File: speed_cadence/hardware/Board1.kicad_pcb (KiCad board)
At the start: 2 copper layers, 32.8 x 58.2 mm, 17 parts, among them IC1 AH1912-W-7, J1 DX07S016JA3R1500, J2 Conn_01x04_Pin, J3 Conn_ST_STDC14, J4 XT60_M_7.2mm, SW1 SW_Push, U1 STM32F042G6U6TR, U2 TS2940CW33_RPG

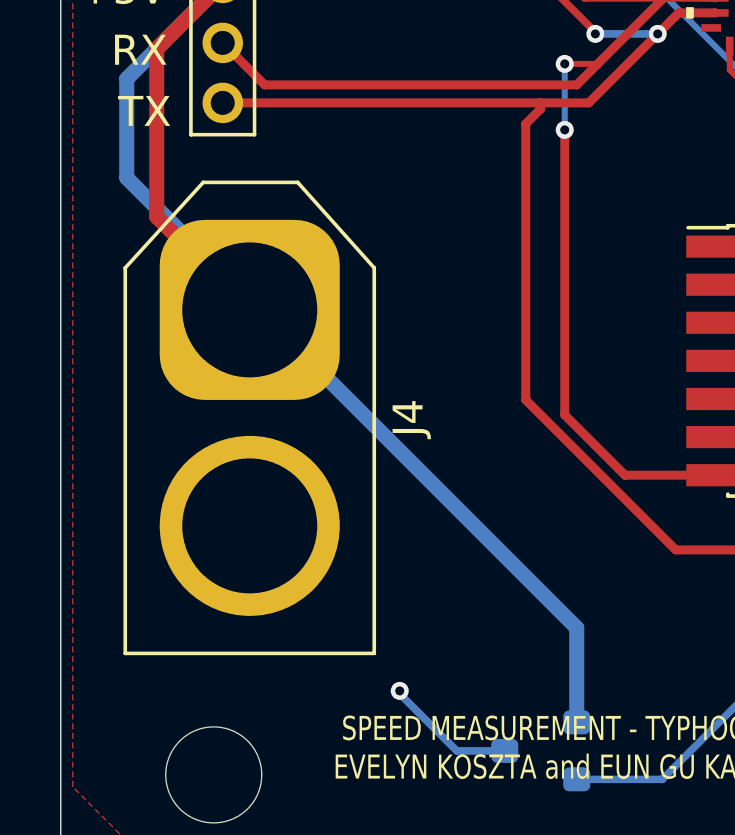
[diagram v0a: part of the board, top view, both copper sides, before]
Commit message: flipped connector
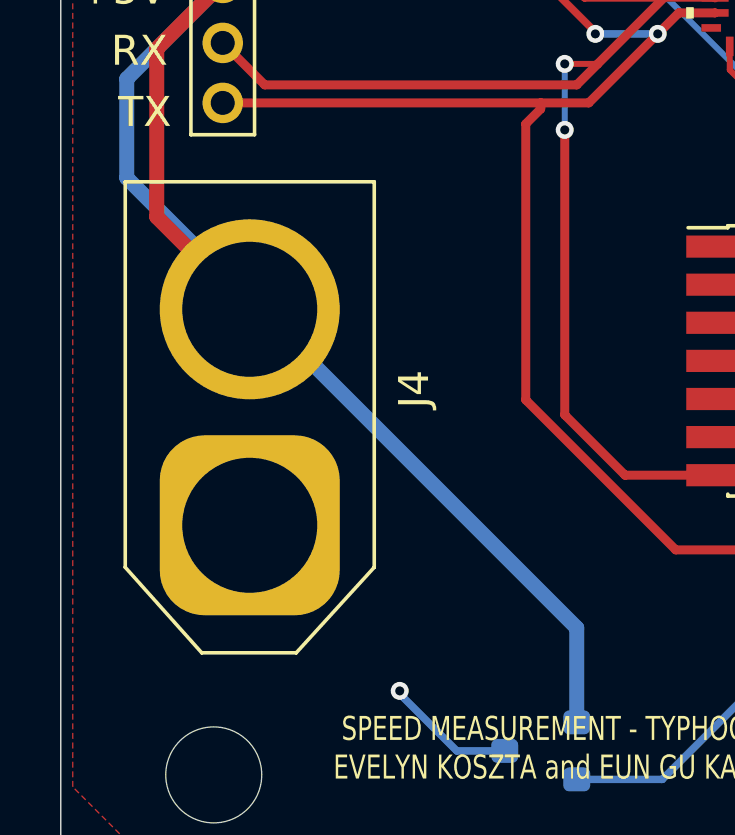
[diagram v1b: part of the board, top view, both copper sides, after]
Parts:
- moved J4 7.18 mm to (75.1, 97.1), turned to 90 degrees
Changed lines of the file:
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@@
 	(footprint "Connector_AMASS:AMASS_XT60-M_1x02_P7.20mm_Vertical"
 		(layer "F.Cu")
-		(at 75.1 89.9 -90)
+		(at 75.1 97.08 90)
 		(descr "AMASS female XT60, through hole, vertical, https://www.tme.eu/Document/2d152ced3b7a446066e6c419d84bb460/XT60%20SPEC.pdf")
 		(tags "XT60 female vertical")
 		(property "Reference" "J4"
-			(at 3.6 -5.3 90)
+			(at 4.54 5.48 270)
 			(layer "F.SilkS")
 			(effects
@@
 		)
 		(property "Value" "XT60_M_7.2mm"
-			(at 3.6 5.4 90)
+			(at 3.6 5.4 270)
 			(layer "F.Fab")
 			(effects
@@
 		)
 		(property "Footprint" "Connector_AMASS:AMASS_XT60-M_1x02_P7.20mm_Vertical"
-			(at 0 0 -90)
+			(at 0 0 90)
 			(unlocked yes)
 			(layer "F.Fab")
@@
 		)
 		(property "Datasheet" ""
-			(at 0 0 -90)
+			(at 0 0 90)
 			(unlocked yes)
 			(layer "F.Fab")
@@
 		)
 		(property "Description" "Generic connector, single row, 01x02, script generated"
-			(at 0 0 -90)
+			(at 0 0 90)
 			(unlocked yes)
 			(layer "F.Fab")
@@
 		(attr through_hole)
 		(fp_line
+			(start 11.45 -4.15)
+			(end -1.4 -4.15)
+			(stroke
+				(width 0.12)
+				(type solid)
+			)
+			(layer "F.SilkS")
+		)
+		(fp_line
+			(start -1.4 -4.15)
+			(end -4.25 -1.6)
+			(stroke
+				(width 0.12)
+				(type solid)
+			)
+			(layer "F.SilkS")
+		)
+		(fp_line
+			(start -4.25 -1.6)
+			(end -4.25 1.55)
+			(stroke
+				(width 0.12)
+				(type solid)
+			)
+			(layer "F.SilkS")
+		)
+		(fp_line
+			(start -4.25 1.55)
+			(end -1.4 4.15)
+			(stroke
+				(width 0.12)
+				(type solid)
+			)
+			(layer "F.SilkS")
+		)
+		(fp_line
+			(start 11.45 4.15)
+			(end 11.45 -4.15)
+			(stroke
+				(width 0.12)
+				(type solid)
+			)
+			(layer "F.SilkS")
+		)
+		(fp_line
 			(start -1.4 4.15)
 			(end 11.45 4.15)
@@
 		)
 		(fp_line
-			(start 11.45 4.15)
-			(end 11.45 -4.15)
-			(stroke
-				(width 0.12)
-				(type solid)
-			)
-			(layer "F.SilkS")
-		)
-		(fp_line
-			(start -4.25 1.55)
-			(end -1.4 4.15)
-			(stroke
-				(width 0.12)
-				(type solid)
-			)
-			(layer "F.SilkS")
-		)
-		(fp_line
-			(start -4.25 -1.6)
-			(end -4.25 1.55)
-			(stroke
-				(width 0.12)
-				(type solid)
-			)
-			(layer "F.SilkS")
-		)
-		(fp_line
-			(start -1.4 -4.15)
-			(end -4.25 -1.6)
-			(stroke
-				(width 0.12)
-				(type solid)
-			)
-			(layer "F.SilkS")
-		)
-		(fp_line
-			(start 11.45 -4.15)
-			(end -1.4 -4.15)
-			(stroke
-				(width 0.12)
-				(type solid)
-			)
-			(layer "F.SilkS")
+			(start 11.85 -4.6)
+			(end 11.85 4.6)
+			(stroke
+				(width 0.05)
+				(type solid)
+			)
+			(layer "F.CrtYd")
+		)
+		(fp_line
+			(start -1.6 -4.6)
+			(end 11.85 -4.6)
+			(stroke
+				(width 0.05)
+				(type solid)
+			)
+			(layer "F.CrtYd")
+		)
+		(fp_line
+			(start -4.65 -1.85)
+			(end -1.6 -4.6)
+			(stroke
+				(width 0.05)
+				(type solid)
+			)
+			(layer "F.CrtYd")
+		)
+		(fp_line
+			(start -4.65 1.85)
+			(end -4.65 -1.85)
+			(stroke
+				(width 0.05)
+				(type solid)
+			)
+			(layer "F.CrtYd")
+		)
+		(fp_line
+			(start 11.85 4.6)
+			(end -1.6 4.6)
+			(stroke
+				(width 0.05)
+				(type solid)
+			)
+			(layer "F.CrtYd")
 		)
 		(fp_line
@@
 		)
 		(fp_line
-			(start 11.85 4.6)
-			(end -1.6 4.6)
-			(stroke
-				(width 0.05)
-				(type solid)
-			)
-			(layer "F.CrtYd")
-		)
-		(fp_line
-			(start -4.65 1.85)
-			(end -4.65 -1.85)
-			(stroke
-				(width 0.05)
-				(type solid)
-			)
-			(layer "F.CrtYd")
-		)
-		(fp_line
-			(start -4.65 -1.85)
-			(end -1.6 -4.6)
-			(stroke
-				(width 0.05)
-				(type solid)
-			)
-			(layer "F.CrtYd")
-		)
-		(fp_line
-			(start -1.6 -4.6)
-			(end 11.85 -4.6)
-			(stroke
-				(width 0.05)
-				(type solid)
-			)
-			(layer "F.CrtYd")
-		)
-		(fp_line
-			(start 11.85 -4.6)
-			(end 11.85 4.6)
-			(stroke
-				(width 0.05)
-				(type solid)
-			)
-			(layer "F.CrtYd")
+			(start 11.35 -4.05)
+			(end -1.4 -4.05)
+			(stroke
+				(width 0.12)
+				(type solid)
+			)
+			(layer "F.Fab")
+		)
+		(fp_line
+			(start -1.4 -4.05)
+			(end -4.15 -1.55)
+			(stroke
+				(width 0.12)
+				(type solid)
+			)
+			(layer "F.Fab")
+		)
+		(fp_line
+			(start -4.15 -1.55)
+			(end -4.15 1.55)
+			(stroke
+				(width 0.12)
+				(type solid)
+			)
+			(layer "F.Fab")
+		)
+		(fp_line
+			(start -4.15 1.55)
+			(end -1.4 4.05)
+			(stroke
+				(width 0.12)
+				(type solid)
+			)
+			(layer "F.Fab")
+		)
+		(fp_line
+			(start 11.35 4.05)
+			(end 11.35 -4.05)
+			(stroke
+				(width 0.12)
+				(type solid)
+			)
+			(layer "F.Fab")
 		)
 		(fp_line
@@
 			(layer "F.Fab")
 		)
-		(fp_line
-			(start 11.35 4.05)
-			(end 11.35 -4.05)
-			(stroke
-				(width 0.12)
-				(type solid)
-			)
-			(layer "F.Fab")
-		)
-		(fp_line
-			(start -4.15 1.55)
-			(end -1.4 4.05)
-			(stroke
-				(width 0.12)
-				(type solid)
-			)
-			(layer "F.Fab")
-		)
-		(fp_line
-			(start -4.15 -1.55)
-			(end -4.15 1.55)
-			(stroke
-				(width 0.12)
-				(type solid)
-			)
-			(layer "F.Fab")
-		)
-		(fp_line
-			(start -1.4 -4.05)
-			(end -4.15 -1.55)
-			(stroke
-				(width 0.12)
-				(type solid)
-			)
-			(layer "F.Fab")
-		)
-		(fp_line
-			(start 11.35 -4.05)
-			(end -1.4 -4.05)
-			(stroke
-				(width 0.12)
-				(type solid)
-			)
-			(layer "F.Fab")
-		)
 		(fp_text user "${REFERENCE}"
-			(at 3.6 0.05 90)
+			(at 3.6 0.05 270)
 			(layer "F.Fab")
 			(effects
@@
 		)
 		(pad "1" thru_hole roundrect
-			(at 0 0 270)
+			(at 0 0 90)
 			(size 6 6)
 			(drill 4.5)
@@
 		)
 		(pad "2" thru_hole circle
-			(at 7.2 0 270)
+			(at 7.2 0 90)
 			(size 6 6)
 			(drill 4.5)

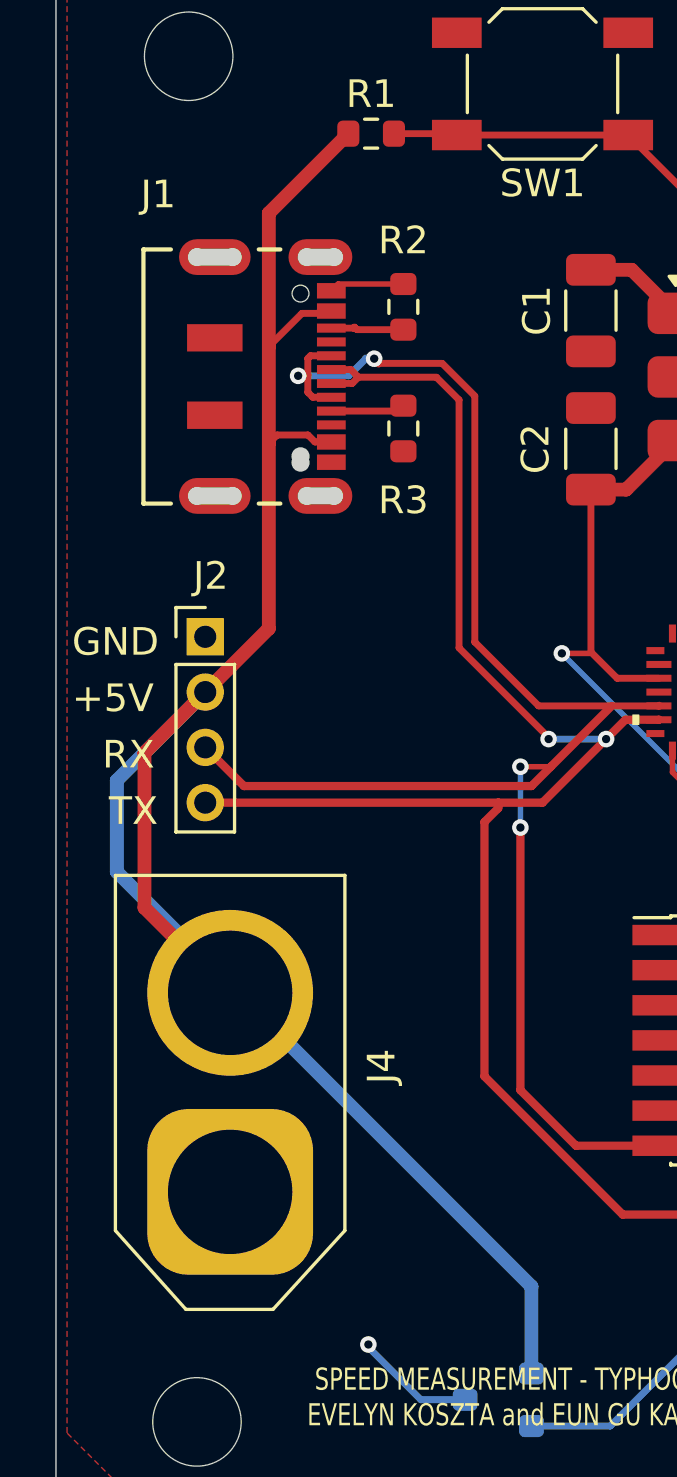
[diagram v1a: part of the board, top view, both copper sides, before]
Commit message: Removed battery connector
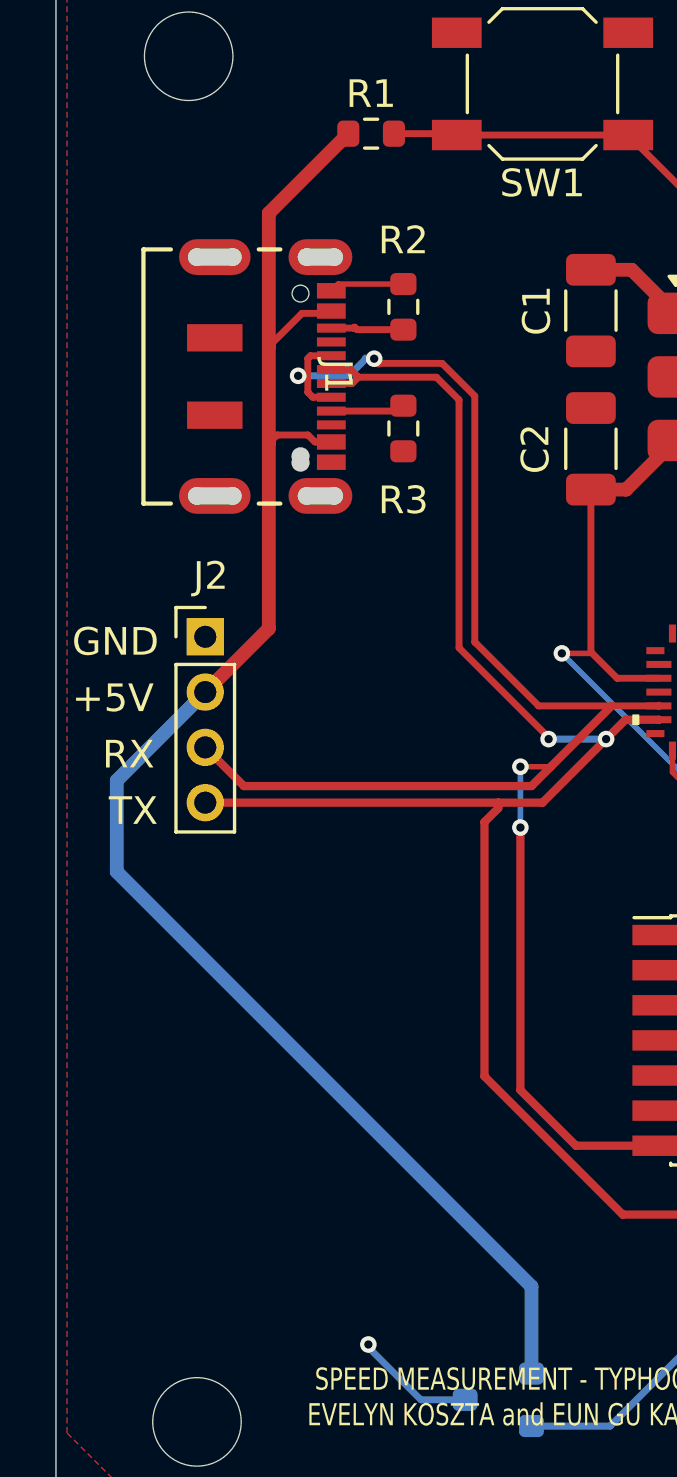
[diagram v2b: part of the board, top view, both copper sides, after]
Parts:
- removed J4: XT60_M_7.2mm, Connector_AMASS:AMASS_XT60-M_1x02_P7.20mm_Vertical
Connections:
- net + BATT renamed +5V
- net - BATT renamed GND
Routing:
- net +5V: track 76.6 -> 63.5 mm

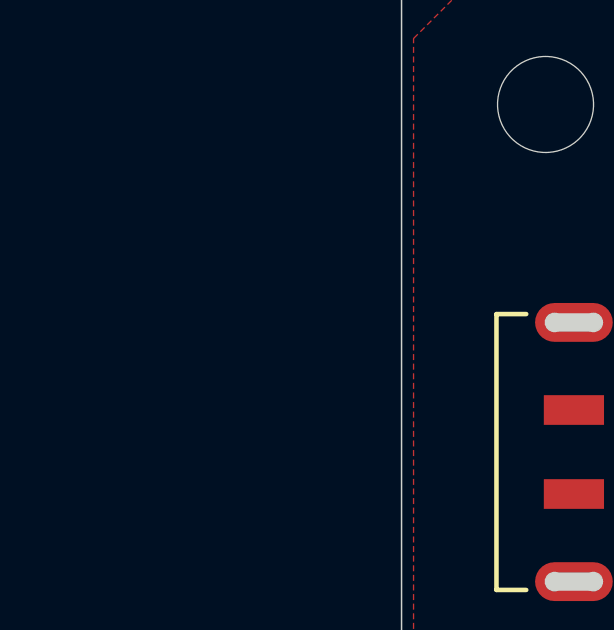
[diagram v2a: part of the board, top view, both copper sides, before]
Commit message: Added the CAN transciever
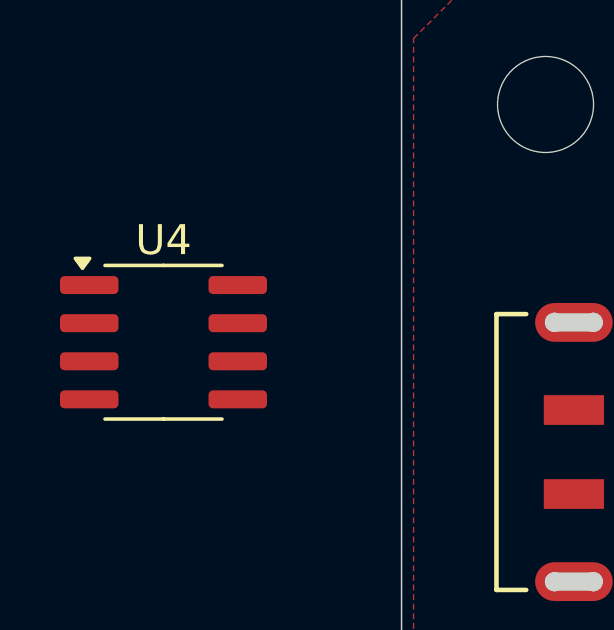
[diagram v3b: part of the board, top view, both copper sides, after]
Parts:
- added U4: TJA1051T-3, Package_SO:SOIC-8_3.9x4.9mm_P1.27mm, F.Cu at (60.9, 63.9)
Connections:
- J2 pad 3: CAN_RX -> CAN_H
- J2 pad 4: CAN_TX -> CAN_L

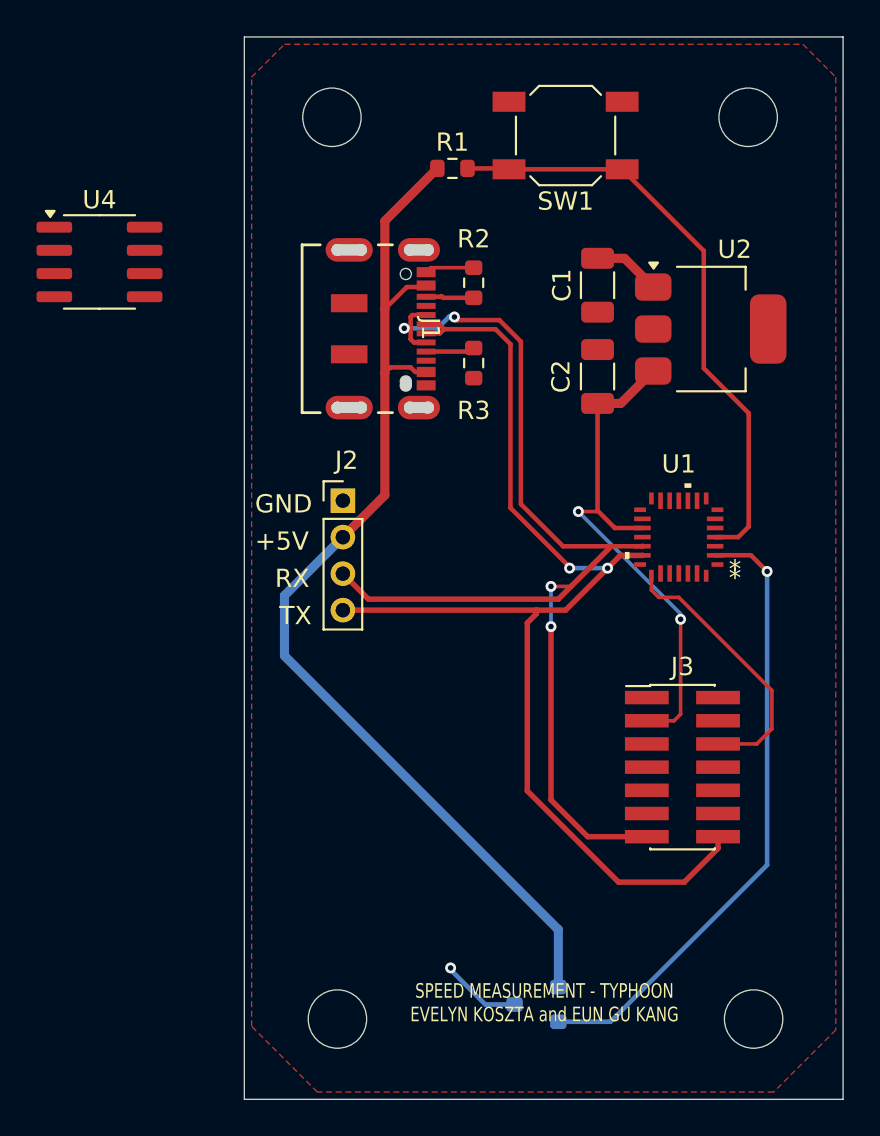
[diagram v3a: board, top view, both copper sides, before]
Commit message: Updated PCB with refined connections and transciever
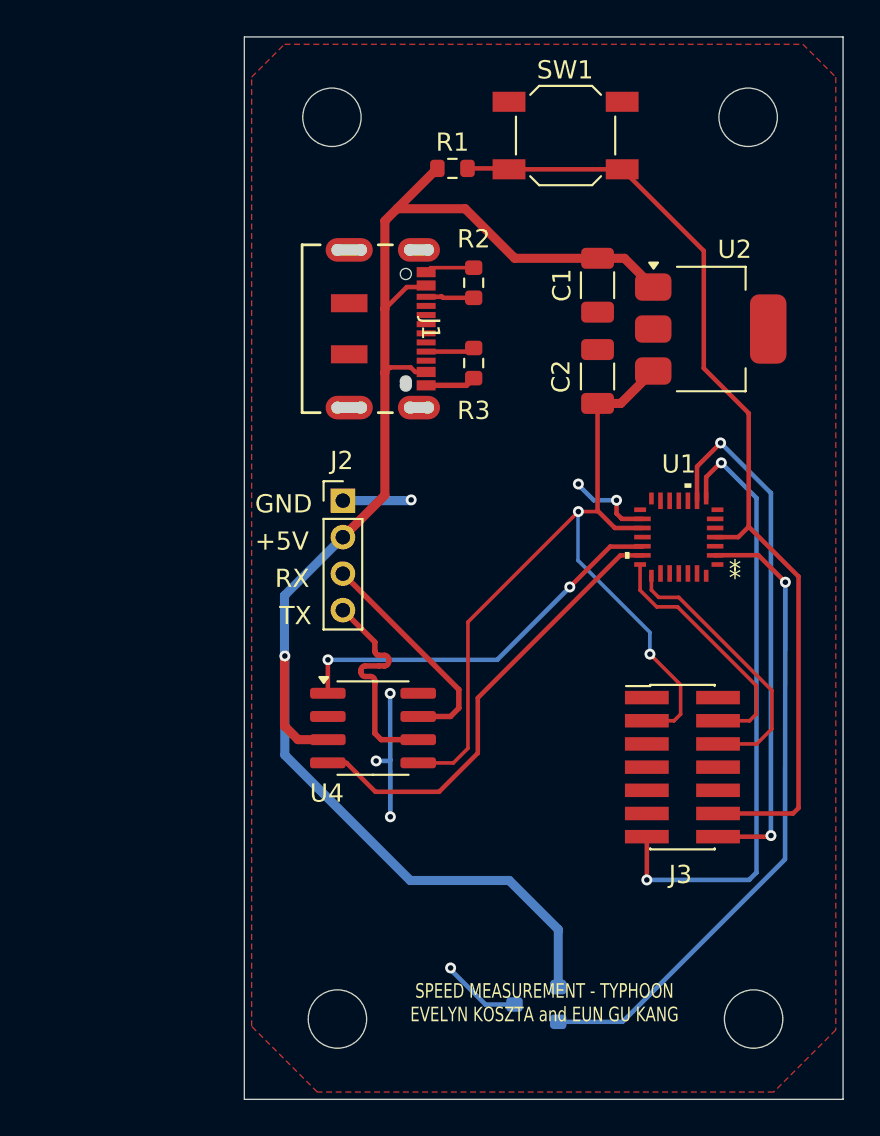
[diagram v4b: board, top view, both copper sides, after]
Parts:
- moved U4 29.6 mm to (75.8, 89.5)
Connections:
- J1 pad 5: CAN_RX -> unconnected-(J1-D--Pad5)
- J1 pad 6: CAN_TX -> unconnected-(J1-D+-Pad6)
- J1 pad 7: CAN_TX -> unconnected-(J1-D+-Pad7)
- J1 pad 8: CAN_RX -> unconnected-(J1-D--Pad8)
- J3 pad 13: CAN_RX -> Prog_RX
- J3 pad 14: CAN_TX -> Prog_TX
- U1 pad 19: CAN_RX -> CAN_TX
- U1 pad 20: CAN_TX -> CAN_RX
- U1 pad 8: unconnected-(U1A-PA2-Pad8) -> Prog_RX
- U1 pad 9: unconnected-(U1A-PA3-Pad9) -> Prog_TX
- U4 pad 5: unconnected-(U4-VIO-Pad5) -> +3V3
- U4 pad 8: unconnected-(U4-S-Pad8) -> GND
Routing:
- net CAN_TX: track 63.6 -> 21.8 mm
- net CAN_RX: track 62.8 -> 25.0 mm, vias 4 -> 0
- net Prog_RX: track 0.00 -> 34.2 mm, vias 0 -> 2
- net Prog_TX: track 0.00 -> 29.5 mm, vias 0 -> 2
- net +5V: track 63.5 -> 85.3 mm, vias 0 -> 1
- net RESET_PROG: track 33.0 -> 54.1 mm
- net GND: track 7.33 -> 26.4 mm, vias 1 -> 7
- net +3V3: track 29.1 -> 47.6 mm
- net codeio: track 0.00 -> 13.7 mm
- net CAN_H: track 0.00 -> 12.4 mm
- net CAN_L: track 0.00 -> 12.4 mm
- net Net-(IC1-OUTPUT): track 34.3 -> 35.8 mm
